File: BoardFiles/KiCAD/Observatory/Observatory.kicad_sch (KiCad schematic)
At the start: 28 parts, among them J10 Dio_Jump, J11 nRF Connections, J12 Sulu Header, J13 Serial, J14 RsTx_Dio, J15 RsRx_Dio, J16 JScope Voltage, J20 Mounting Hole, J21 Mounting Hole, J22 Mounting Hole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

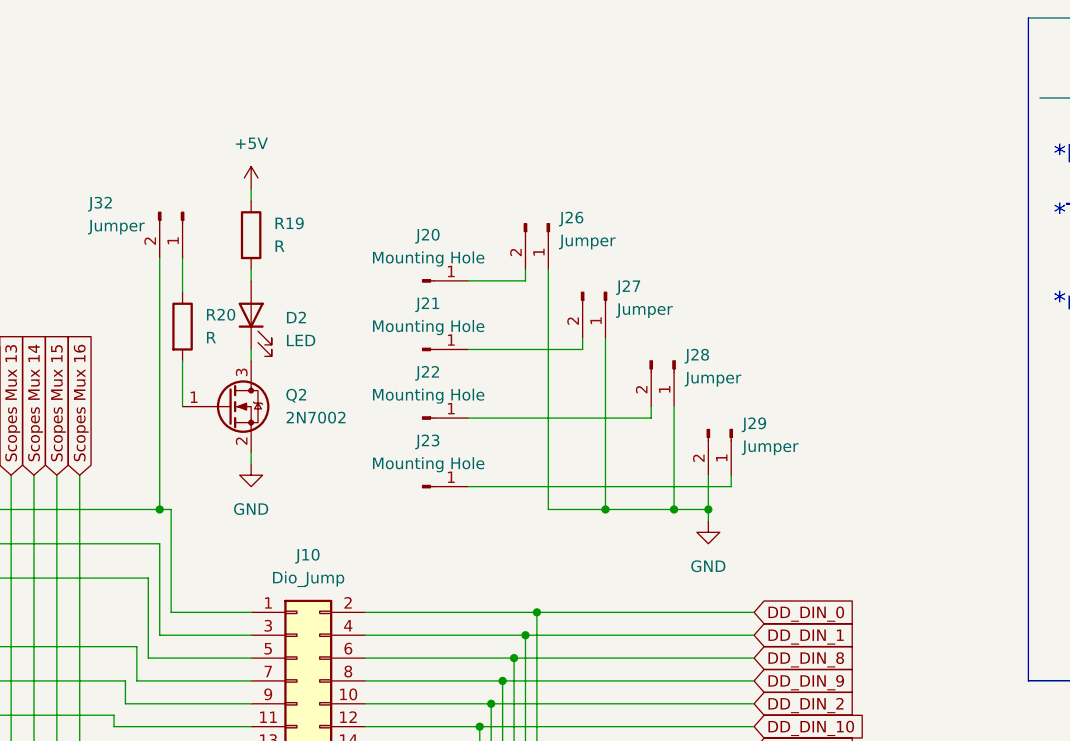
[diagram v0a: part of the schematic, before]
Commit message: LED circuit fix, added decoupling cap
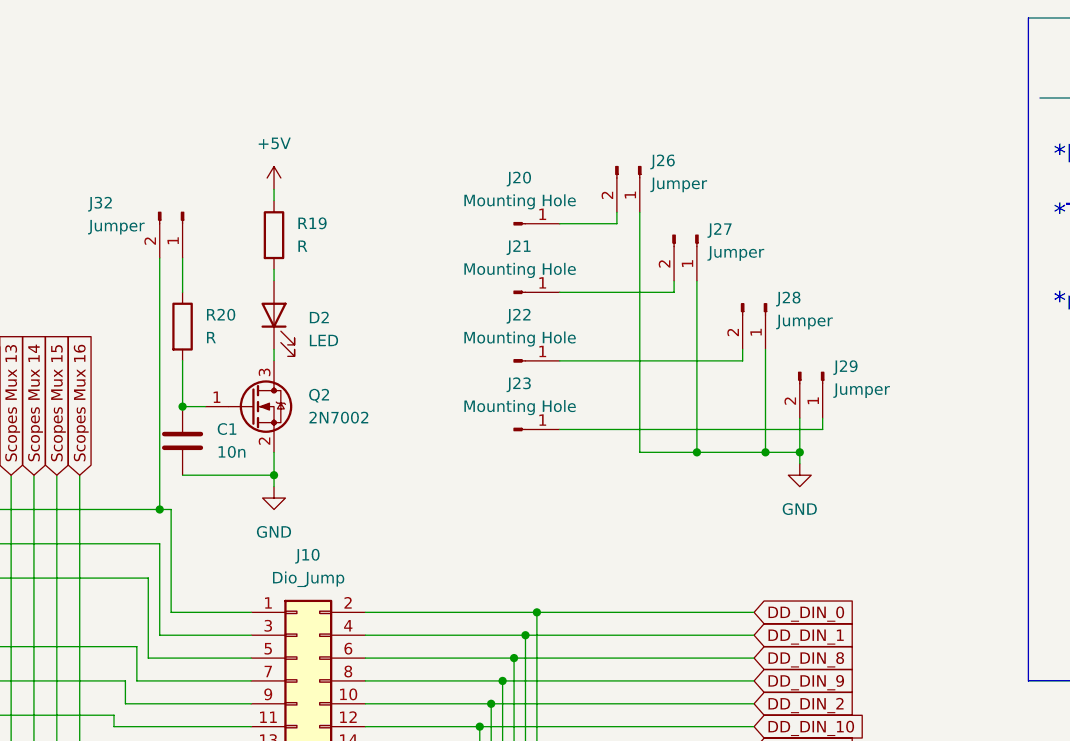
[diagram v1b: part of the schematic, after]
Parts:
- added C1: 10n, Capacitor_SMD:C_0805_2012Metric_Pad1.18x1.45mm_HandSolder, symbol Device:C
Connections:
- net GND: now also C1.2
- net at Q2.1 (G), R20.2: now also C1.1
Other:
- moved on the sheet: D2, J20, J21, J22, J23, J26, J27, J28, J29, Q2, R19

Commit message: REV3 begin
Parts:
- removed J14: RsTx_Dio, Connector_PinHeader_2.54mm:PinHeader_1x02_P2.54mm_Vertical, symbol Connector:Conn_01x02_Pin
- removed J15: RsRx_Dio, Connector_PinHeader_2.54mm:PinHeader_1x02_P2.54mm_Vertical, symbol Connector:Conn_01x02_Pin
- removed SW1, SW2: SW_DIP_x08, Button_Switch_SMD:SW_DIP_SPSTx08_Slide_6.7x21.88mm_W8.61mm_P2.54mm_LowProfile, symbol Switch:SW_DIP_x08
- J11: footprint Connector_PinHeader_2.54mm:PinHeader_1x06_P2.54mm_Vertical -> Connector_PinHeader_2.54mm:PinHeader_1x06_P2.54mm_Horizontal
- J13, J9: footprint Connector_PinHeader_2.54mm:PinHeader_1x02_P2.54mm_Vertical -> Connector_PinHeader_2.54mm:PinHeader_1x02_P2.54mm_Horizontal
- J24: footprint Connector_PinHeader_2.54mm:PinHeader_1x03_P2.54mm_Vertical -> Button_Switch_THT:SW_CK_JS202011CQN_DPDT_Straight
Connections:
- net DD_DIN_0: now also J10.4 (Pin_4); no longer J10.2 (Pin_2)
- net DD_DIN_1: now also J10.2 (Pin_2); no longer J10.4 (Pin_4)

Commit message: REV3 DRC pass
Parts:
- removed C1: 10n, Capacitor_SMD:C_0805_2012Metric_Pad1.18x1.45mm_HandSolder, symbol Device:C
- removed D2: LED, LED_SMD:LED_0805_2012Metric_Pad1.15x1.40mm_HandSolder, symbol Device:LED
- removed J26, J27, J28, J29: Jumper, Jumper:SolderJumper-2_P1.3mm_Open_Pad1.0x1.5mm, symbol Connector:Conn_01x02_Pin
- removed Q2: 2N7002, Package_TO_SOT_SMD:SOT-23, symbol Transistor_FET:2N7002
- removed R19, R20: R, Resistor_SMD:R_0805_2012Metric_Pad1.20x1.40mm_HandSolder, symbol Device:R
- added J36, J37: Mounting Hole, MountingHole:MountingHole_3.2mm_M3_Pad_Via, symbol Connector:Conn_01x01_Pin
- J11: footprint Connector_PinHeader_2.54mm:PinHeader_1x06_P2.54mm_Horizontal -> Connector_PinHeader_2.54mm:PinHeader_1x06_P2.54mm_Vertical
- J13, J9: footprint Connector_PinHeader_2.54mm:PinHeader_1x02_P2.54mm_Horizontal -> Connector_PinHeader_2.54mm:PinHeader_1x02_P2.54mm_Vertical
- J24: value prog. LED -> Observatory PWR
- J32: footprint Jumper:SolderJumper-2_P1.3mm_Open_Pad1.0x1.5mm -> Jumper:SolderJumper-2_P1.3mm_Bridged_RoundedPad1.0x1.5mm
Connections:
- net Scopes Mux  25 is gone; now on net Scopes Mux  23: J12.16 (Pin_16), U1.16c (IMU_VDD)
- net +5V: now also J12.12 (Pin_12), J12.9 (Pin_9), J16.5 (Pin_5), J32.1 (Pin_1), U1.12c (EXT_BAT), U1.9c (EXT_BAT)
- net AD_DC_Supply+: now also J24.3 (Pin_3); no longer J24.1 (Pin_1)
- net GND: now also J20.1 (Pin_1), J21.1 (Pin_1), J22.1 (Pin_1), J23.1 (Pin_1), J36.1 (Pin_1), J37.1 (Pin_1)
- net Scopes Mux  1: no longer J32.2 (Pin_2)
- net Scopes Mux  10: now also J10.19 (Pin_19), U1.12a (GPIO12); no longer J10.17 (Pin_17), U1.11a (GPIO4)
- net Scopes Mux  11: now also J10.21 (Pin_21), U1.13a (GPIO5); no longer J10.15 (Pin_15), U1.10a (GPIO11)
- net Scopes Mux  12: now also J10.23 (Pin_23), U1.14a (GPIO13); no longer J10.13 (Pin_13), U1.9a (GPIO3)
- net Scopes Mux  17: now also J12.21 (Pin_21), U1.21c (ADC_IN); no longer J12.4 (Pin_4), J16.3 (Pin_3), U1.4c (1.8V)
- net Scopes Mux  18: now also J12.22 (Pin_22), U1.22c (ADC_OUT); no longer J12.5 (Pin_5), U1.5c (VBAT)
- net Scopes Mux  19: now also J12.19 (Pin_19), U1.19c (VDDD); no longer J12.7 (Pin_7), U1.7c (VDDD)
- net Scopes Mux  20: now also J12.20 (Pin_20), U1.20c (BTSRC_SEL); no longer J12.8 (Pin_8), J16.1 (Pin_1), U1.8c (1.1V)
- net Scopes Mux  21: now also J12.17 (Pin_17), U1.17c (VBAT); no longer J12.9 (Pin_9), U1.9c (EXT_BAT)
- net Scopes Mux  22: now also J12.18 (Pin_18), U1.18c (VDDIO); no longer J12.10 (Pin_10), U1.10c (1.1V_IN)
- net Scopes Mux  23: no longer J12.13 (Pin_13), U1.13c (VDDIO)
- net Scopes Mux  26: now also J32.2 (Pin_2); no longer J12.18 (Pin_18), U1.18c (VDDIO)
- net Scopes Mux  27: now also J12.7 (Pin_7), U1.7c (VDDD); no longer J12.20 (Pin_20), U1.20c (BTSRC_SEL)
- net Scopes Mux  28: now also J12.8 (Pin_8), J16.1 (Pin_1), U1.8c (1.1V); no longer J12.21 (Pin_21), U1.21c (ADC_IN)
- net Scopes Mux  29: now also J12.6 (Pin_6), U1.6c (1.8V); no longer J12.22 (Pin_22), U1.22c (ADC_OUT)
- net Scopes Mux  7: now also J10.13 (Pin_13), U1.9a (GPIO3); no longer J10.23 (Pin_23), U1.14a (GPIO13)
- net Scopes Mux  8: now also J10.15 (Pin_15), U1.10a (GPIO11); no longer J10.21 (Pin_21), U1.13a (GPIO5)
- net Scopes Mux  9: now also J10.17 (Pin_17), U1.11a (GPIO4); no longer J10.19 (Pin_19), U1.12a (GPIO12)
- new net: J12.10 (Pin_10), U1.10c (1.1V_IN)
- new net: J12.13 (Pin_13), U1.13c (VDDIO)
- new net: J12.4 (Pin_4), J16.3 (Pin_3), U1.4c (1.8V)
- new net: J12.5 (Pin_5), U1.5c (VBAT)
- new net: J24.1 (Pin_1), J9.2 (Pin_2)
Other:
- moved on the sheet: J20, J21, J22, J23, J24

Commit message: REV3 complete
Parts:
- added J4: GPIO Expand, Connector_PinHeader_2.54mm:PinHeader_2x10_P2.54mm_Vertical, symbol Connector_Generic:Conn_02x10_Odd_Even
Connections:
- net GND: now also J4.1 (Pin_1), J4.19 (Pin_19), J4.20 (Pin_20)
- net Scopes Mux  1: now also J4.2 (Pin_2)
- net Scopes Mux  10: now also J4.12 (Pin_12)
- net Scopes Mux  11: now also J4.13 (Pin_13)
- net Scopes Mux  12: now also J4.14 (Pin_14)
- net Scopes Mux  13: now also J4.15 (Pin_15)
- net Scopes Mux  14: now also J4.16 (Pin_16)
- net Scopes Mux  15: now also J4.17 (Pin_17)
- net Scopes Mux  16: now also J4.18 (Pin_18)
- net Scopes Mux  2: now also J4.3 (Pin_3)
- net Scopes Mux  3: now also J4.4 (Pin_4)
- net Scopes Mux  4: now also J4.6 (Pin_6)
- net Scopes Mux  5: now also J4.7 (Pin_7)
- net Scopes Mux  6: now also J4.8 (Pin_8)
- net Scopes Mux  7: now also J4.9 (Pin_9)
- net Scopes Mux  8: now also J4.10 (Pin_10)
- net Scopes Mux  9: now also J4.11 (Pin_11)
- net at U1.5a (GPIO1): now also J4.5 (Pin_5)
- no-connect marks 8 -> 7

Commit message: REV3.1 done. Labels fixed, reverse polarity protection added. Layout impoved.
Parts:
- added J34: Jumper, Jumper:SolderJumper-2_P1.3mm_Open_Pad1.0x1.5mm, symbol Connector:Conn_01x02_Pin
- added R19: R_st, Resistor_SMD:R_0805_2012Metric_Pad1.20x1.40mm_HandSolder, symbol Device:R
- added U2: LM66100DCKR, 3rdPrty_Footprints:LM66100DCKR, symbol 3rdPrty_Symbols:LM66100DCKR
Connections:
- net GND: now also U2.2 (GND), U2.3 (*CE)
- net at J24.1 (Pin_1): now also J34.1 (Pin_1), R19.1, U2.6 (VOUT); no longer J9.2 (Pin_2)
- new net: J34.2 (Pin_2), J9.2 (Pin_2), U2.1 (VIN)
- new net: R19.2, U2.5 (ST)
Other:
- removed sheet Mux Config
- removed sheet RF Explorer
- note added: "*n_RF Connections https://crystalfree.atlassian.net/wiki/spaces/SCUM/pages/1901559821/Sulu+Programming+With+nRF+Setup"
- note removed: "*LED needs to change footprint. (OSRAM SFH4555) *There is more to the LED circuit than previously thought. Currently unable to find any schematic, only a photo with companant labels but to connections. *n_RF Connections https://crystalfree.atlassian.net/wiki/spaces/SCUM/pages/1901559821/Sulu+Programming+With+nRF+Setup"
- moved on the sheet: D1, J10, J11, J12, J13, J16, J20, J21, J22, J23, J24, J32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
